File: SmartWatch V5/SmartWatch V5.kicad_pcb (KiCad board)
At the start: 4 copper layers, 23.7 x 34.2 mm, 55 parts, among them J1 10118192-0001LF, J10 TestPad, J2 , J8 TestPad, J9 TestPad, Q1 FDN340P, Q2 MMBT3904, Q3 MMBT3904, Q4 FDN028N20, Q5 FDN028N20, Q6 FDN028N20, SW1 EVQ-P7J01P, SW2 EVQ-P7J01P, U1 MAX17260, U10 TSC2003IPWR, U2 FT231XQ, U3 LP5912-3.3DRVT, U5 MCP73832-2-OT, U6 ESP32-WROOM-32, U8 ADXL337

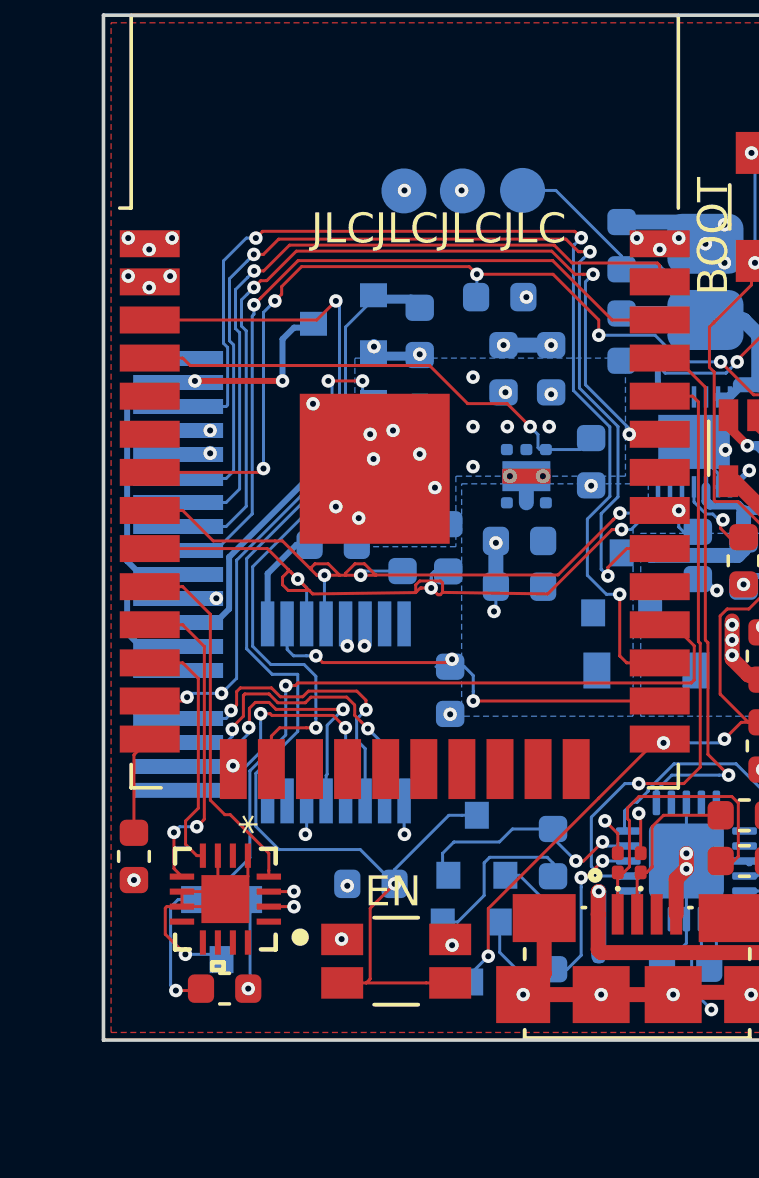
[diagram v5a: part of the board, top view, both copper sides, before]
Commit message: Added additional capacitence where board space permits
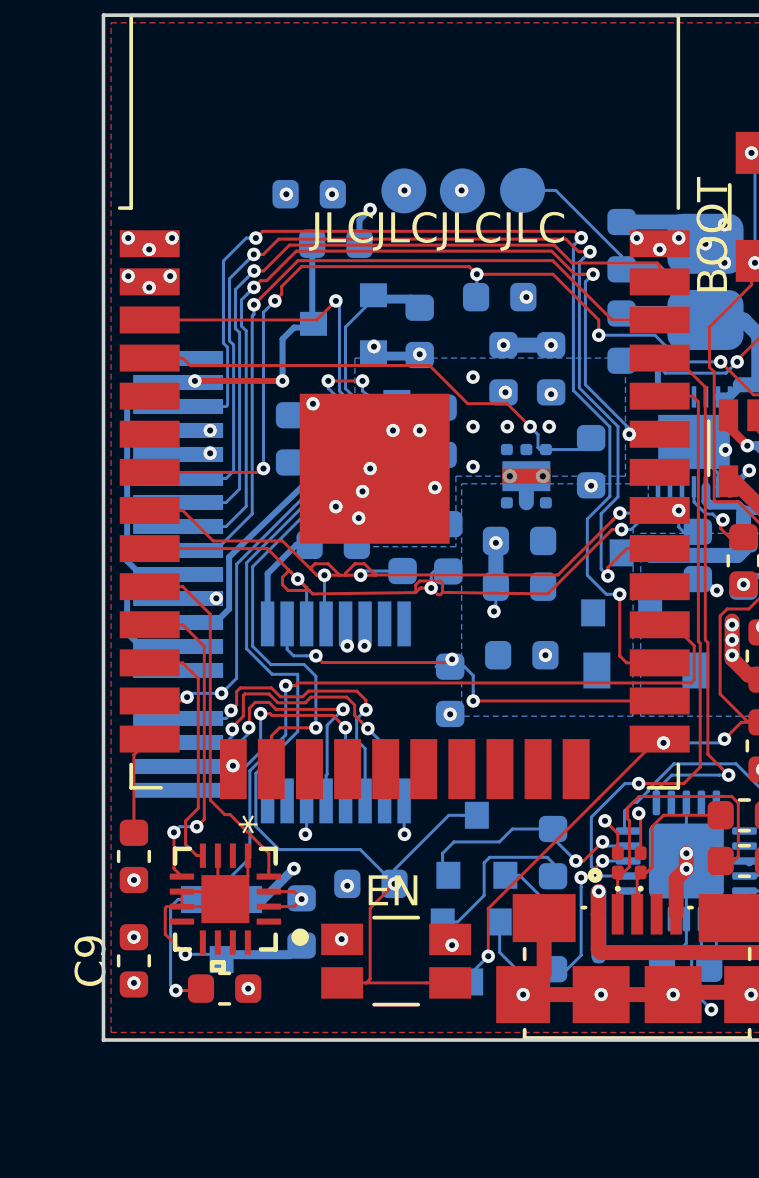
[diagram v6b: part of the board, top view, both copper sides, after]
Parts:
- added C12: 10uF, Capacitor_SMD:C_0603_1608Metric, B.Cu at (87.8, 71.6)
- added C13: 10uF, Capacitor_SMD:C_0603_1608Metric, B.Cu at (87.5, 95.9)
- added C14: 10uF, Capacitor_SMD:C_0603_1608Metric, B.Cu at (88.6, 73.3)
- added C15: 10uF, Capacitor_SMD:C_0603_1608Metric, B.Cu at (87.1, 79.8)
- added C6: 10uF, Capacitor_SMD:C_0603_1608Metric, B.Cu at (94.8, 87.0)
- added C9: 10uF, Capacitor_SMD:C_0603_1608Metric, F.Cu at (81.9, 97.2)
- moved Q6 0.78 mm to (89.7, 79.5)
- moved R22 0.76 mm to (92.2, 79.5)
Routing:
- net /LCD_PWR: track 18.8 -> 21.5 mm
- net /LCD_CATHODE: track 9.00 -> 11.5 mm
- net /ACCEL_PWR: track 10.2 -> 12.6 mm
- net /LCD_LED: track 18.1 -> 19.7 mm
- net GND: track 52.0 -> 53.2 mm, vias 48 -> 53
- net /LCD_EN: track 21.7 -> 22.7 mm
- net +3V3: track 11.3 -> 12.1 mm, vias 24 -> 25
- net /EN: track 43.8 -> 44.4 mm

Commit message: Final Touches to Board Design
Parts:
- moved R22 0.25 mm to (92.2, 79.3)
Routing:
- net GND: track 53.2 -> 54.5 mm, vias 53 -> 52
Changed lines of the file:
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@@
     (thickness 1.6)
     (drawings 17)
-    (tracks 911)
+    (tracks 914)
     (zones 0)
     (modules 61)
@@
     (40 Dwgs.User user hide)
     (41 Cmts.User user hide)
-    (42 Eco1.User user hide)
-    (43 Eco2.User user hide)
+    (42 Eco1.User user)
+    (43 Eco2.User user)
     (44 Edge.Cuts user)
-    (45 Margin user hide)
+    (45 Margin user)
     (46 B.CrtYd user)
     (47 F.CrtYd user)
-    (48 B.Fab user hide)
+    (48 B.Fab user)
     (49 F.Fab user hide)
   )
   (setup
-    (last_trace_width 0.2)
+    (last_trace_width 0.3)
     (user_trace_width 0.1)
     (user_trace_width 0.12)
@@
   )
   (module Resistor_SMD:R_0603_1608Metric (layer B.Cu)
-    (at 92.202 79.5275 270)
+    (at 92.202 79.2735 270)
     (descr "Resistor SMD 0603 (1608 Metric), square (rectangular) end terminal, IPC_7351 nominal, (Body size source: http://www.tortai-tech.com/upload/download/2011102023233369053.pdf), generated with kicad-footprint-generator")
     (tags resistor)
@@
   (via (at 81.915 96.393) (size 0.45) (drill 0.2) (layers F.Cu B.Cu) (net 13))
   (via (at 88.646 82.042) (size 0.45) (drill 0.2) (layers F.Cu B.Cu) (net 13))
-  (via (at 91.948 81.407) (size 0.45) (drill 0.2) (layers F.Cu B.Cu) (net 13))
   (via (at 87.884 78.613) (size 0.45) (drill 0.2) (layers F.Cu B.Cu) (net 13))
   (via (at 90.551 79.502) (size 0.45) (drill 0.2) (layers F.Cu B.Cu) (net 13))
@@
   (via (at 87.249 94.107) (size 0.45) (drill 0.2) (layers F.Cu B.Cu) (net 13))
   (segment (start 86.217 95.139) (end 87.249 94.107) (width 0.3) (layer B.Cu) (net 13))
-  (segment (start 92.065 80.452) (end 92.202 80.315) (width 0.3) (layer B.Cu) (net 13))
-  (segment (start 90.678 80.452) (end 92.065 80.452) (width 0.3) (layer B.Cu) (net 13))
   (segment (start 87.503 78.994) (end 87.884 78.613) (width 0.2) (layer B.Cu) (net 13))
   (segment (start 87.122 78.994) (end 87.503 78.994) (width 0.2) (layer B.Cu) (net 13))
@@
   (segment (start 89.4335 73.279) (end 89.4335 72.4915) (width 0.2) (layer B.Cu) (net 13))
   (segment (start 89.4335 72.4915) (end 89.789 72.136) (width 0.2) (layer B.Cu) (net 13))
+  (segment (start 90.358 80.772) (end 90.678 80.452) (width 0.2) (layer B.Cu) (net 13))
+  (segment (start 89.789 80.772) (end 90.358 80.772) (width 0.2) (layer B.Cu) (net 13))
+  (segment (start 90.678 80.452) (end 90.678 80.452) (width 0.2) (layer B.Cu) (net 13))
+  (segment (start 92.1005 80.4165) (end 92.202 80.315) (width 0.3) (layer B.Cu) (net 13))
+  (segment (start 91.811 80.452) (end 92.202 80.061) (width 0.3) (layer B.Cu) (net 13))
+  (segment (start 90.678 80.452) (end 91.811 80.452) (width 0.3) (layer B.Cu) (net 13))
   (segment (start 103.505 77.978) (end 103.505 78.9455) (width 0.5) (layer B.Cu) (net 14))
   (segment (start 102.124 78.020601) (end 102.124 77.978) (width 0.3) (layer B.Cu) (net 14))
@@
     (polygon
       (pts
-        (xy 98.298 81.026) (xy 92.6465 81.026) (xy 92.6465 83.3755) (xy 89.281 83.3755) (xy 89.281 77.089)
+        (xy 98.298 81.407) (xy 92.6465 81.407) (xy 92.6465 83.3755) (xy 89.281 83.3755) (xy 89.281 77.089)
         (xy 98.298 77.089)
       )
@@
     (polygon
       (pts
-        (xy 99.06 82.423) (xy 98.552 82.423) (xy 98.552 89.027) (xy 92.837 89.027) (xy 92.837 81.28)
-        (xy 99.06 81.28)
+        (xy 99.06 82.423) (xy 98.552 82.423) (xy 98.552 89.027) (xy 92.837 89.027) (xy 92.837 81.661)
+        (xy 99.06 81.661)
       )
     )
